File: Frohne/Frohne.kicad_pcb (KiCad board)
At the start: 4 copper layers, 100 x 100 mm, 215 parts, among them J1 ADC IN, J10 Conn_01x20_Socket, J11 SDR ANT, J12 SDR Out, J2 Conn_02x20_Counter_Clockwise, J3 Conn_02x20_Counter_Clockwise, J4 Conn_01x20_Socket, J5 Conn_01x02, J7 Conn_01x01_Pin, J8 BNC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

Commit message: Unconnected 29
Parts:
- removed J7: Conn_01x01_Pin, Connector_PinHeader_2.54mm:PinHeader_1x01_P2.54mm_Vertical
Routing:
- net GND: track 75.3 -> 120.2 mm
- net +4.7V: track 40.4 -> 54.8 mm
- net Net-(e1-EN): track 9.38 -> 15.2 mm
- net /Raspberry_Pi_Pico/GPIO12: track 13.5 -> 17.1 mm, vias 0 -> 1
- net +3.3V: track 23.6 -> 26.2 mm
- net /Raspberry_Pi_Pico/GPIO13: track 12.5 -> 14.7 mm, vias 0 -> 1
- net Net-(J4-Pin_5): track 0.00 -> 1.62 mm
- net Net-(J4-Pin_19): track 0.00 -> 1.59 mm
- net Net-(J2-Pin_17): track 5.69 -> 7.18 mm

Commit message: Unconnected 16
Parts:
- moved JP50 5.87 mm to (159.2, 33.1)
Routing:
- net Net-(JP19-B): track 22.6 -> 30.8 mm
- net +4.7V: track 54.8 -> 59.0 mm
- net Net-(FB5-Pad1): track 0.08 -> 4.22 mm
- net Net-(J10-Pin_1): track 0.00 -> 3.09 mm
- net Net-(C34-Pad1): track 0.00 -> 1.71 mm
- net Net-(J2-Pin_15): track 4.03 -> 5.69 mm
- net Net-(J4-Pin_2): track 0.00 -> 1.64 mm
- net Net-(J4-Pin_4): track 0.00 -> 1.63 mm
- net Net-(J4-Pin_7): track 0.00 -> 1.63 mm
- net Net-(J4-Pin_6): track 0.00 -> 1.62 mm
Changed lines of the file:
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@@
 	(footprint "Jumper:SolderJumper-2_P1.3mm_Open_RoundedPad1.0x1.5mm"
 		(layer "B.Cu")
-		(at 153.28 33.19 -90)
+		(at 159.15 33.11 -90)
 		(descr "SMD Solder Jumper, 1x1.5mm, rounded Pads, 0.3mm gap, open")
 		(tags "solder jumper open")
@@
 	)
 	(segment
+		(start 159.15 33.76)
+		(end 160.46 33.76)
+		(width 0.6)
+		(layer "B.Cu")
+		(net 13)
+	)
+	(segment
 		(start 161.1 34.06)
 		(end 160.92 34.06)
@@
 	)
 	(segment
+		(start 160.46 33.76)
+		(end 160.84 34.14)
+		(width 0.6)
+		(layer "B.Cu")
+		(net 13)
+	)
+	(segment
+		(start 172.22 32.35)
+		(end 172.035 32.535)
+		(width 0.4)
+		(layer "B.Cu")
+		(net 13)
+	)
+	(segment
 		(start 161.038 33.942)
 		(end 160.84 34.14)
@@
 	)
 	(segment
+		(start 174.31 32.35)
+		(end 172.22 32.35)
+		(width 0.4)
+		(layer "B.Cu")
+		(net 13)
+	)
+	(segment
 		(start 163.85 32.59)
 		(end 163.87 32.57)
@@
 	)
 	(segment
+		(start 121.3085 73.8115)
+		(end 121.3085 69.4615)
+		(width 0.127)
+		(layer "F.Cu")
+		(net 21)
+	)
+	(segment
 		(start 119.81 75.31)
 		(end 119.88 75.24)
@@
 		(net 21)
 	)
+	(segment
+		(start 119.88 75.24)
+		(end 121.3085 73.8115)
+		(width 0.127)
+		(layer "F.Cu")
+		(net 21)
+	)
+	(segment
+		(start 121.3085 69.4615)
+		(end 122.61 68.16)
+		(width 0.127)
+		(layer "F.Cu")
+		(net 21)
+	)
 	(via
 		(at 119.81 76.17)
@@
 	)
 	(segment
+		(start 142.8 45.25)
+		(end 144.35 45.25)
+		(width 0.127)
+		(layer "B.Cu")
+		(net 28)
+	)
+	(segment
+		(start 144.35 45.25)
+		(end 144.4 45.3)
+		(width 0.127)
+		(layer "B.Cu")
+		(net 28)
+	)
+	(segment
 		(start 146.77 125.12)
 		(end 149.56 125.12)
@@
 	)
 	(segment
+		(start 134.62 127.18)
+		(end 134.62 123.13)
+		(width 0.6)
+		(layer "F.Cu")
+		(net 30)
+	)
+	(segment
+		(start 134.62 123.13)
+		(end 134.68 123.07)
+		(width 0.6)
+		(layer "F.Cu")
+		(net 30)
+	)
+	(segment
 		(start 136.43 110.455)
 		(end 134.087 108.112)
@@
 	)
 	(segment
+		(start 126.32 123.88)
+		(end 126.32 122.4)
+		(width 0.127)
+		(layer "F.Cu")
+		(net 80)
+	)
+	(segment
+		(start 126.32 122.4)
+		(end 126.48 122.24)
+		(width 0.127)
+		(layer "F.Cu")
+		(net 80)
+	)
+	(segment
 		(start 128.9 103.94)
 		(end 128.81 103.85)
@@
 	)
 	(segment
+		(start 142.79 47.79)
+		(end 144.35 47.79)
+		(width 0.127)
+		(layer "B.Cu")
+		(net 82)
+	)
+	(segment
+		(start 144.35 47.79)
+		(end 144.4 47.84)
+		(width 0.127)
+		(layer "B.Cu")
+		(net 82)
+	)
+	(segment
 		(start 142.81 60.54)
 		(end 144.4 60.54)
@@
 	)
 	(segment
+		(start 141.51 68.16)
+		(end 139.856 68.16)
+		(width 0.127)
+		(layer "B.Cu")
+		(net 84)
+	)
+	(segment
 		(start 139.844 68.16)
 		(end 139.85 68.166)
@@
 	)
 	(segment
+		(start 139.856 68.16)
+		(end 139.85 68.166)
+		(width 0.127)
+		(layer "B.Cu")
+		(net 84)
+	)
+	(segment
 		(start 142.81 58)
 		(end 144.4 58)
@@
 	)
 	(segment
+		(start 144.36 35.1)
+		(end 144.4 35.14)
+		(width 0.127)
+		(layer "B.Cu")
+		(net 87)
+	)
+	(segment
+		(start 142.78 35.1)
+		(end 144.36 35.1)
+		(width 0.127)
+		(layer "B.Cu")
+		(net 87)
+	)
+	(segment
 		(start 141.51 78.32)
 		(end 135.745 78.32)
@@
 	)
 	(segment
+		(start 144.37 40.25)
+		(end 144.4 40.22)
+		(width 0.127)
+		(layer "B.Cu")
+		(net 95)
+	)
+	(segment
+		(start 142.78 40.25)
+		(end 144.37 40.25)
+		(width 0.127)
+		(layer "B.Cu")
+		(net 95)
+	)
+	(segment
 		(start 137.31 80.866)
 		(end 141.504 80.866)
@@
 	)
 	(segment
-		(start 118.505 126.765)
-		(end 118.53 126.79)
-		(width 0.127)
-		(layer "F.Cu")
-		(net 98)
-	)
-	(segment
 		(start 116.3945 126.7845)
 		(end 116.375 126.765)
@@
 	)
 	(segment
+		(start 159.15 32.46)
+		(end 160.59 32.46)
+		(width 0.6)
+		(layer "B.Cu")
+		(net 113)
+	)
+	(segment
+		(start 160.73 32.6)
+		(end 162.18 32.6)
+		(width 0.6)
+		(layer "B.Cu")
+		(net 113)
+	)
+	(segment
+		(start 160.59 32.46)
+		(end 160.73 32.6)
+		(width 0.6)
+		(layer "B.Cu")
+		(net 113)
+	)
+	(segment

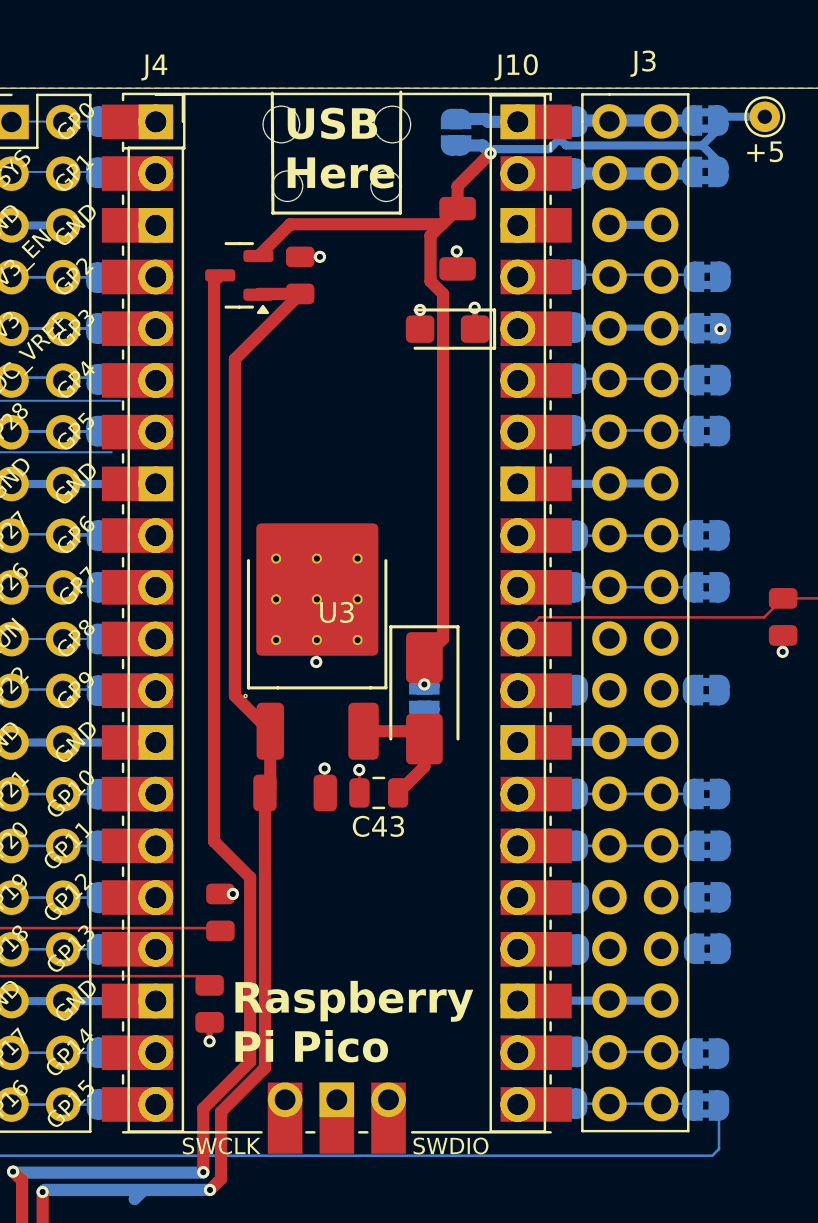
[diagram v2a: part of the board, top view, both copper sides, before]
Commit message: 0 Unconnected 53 Errors
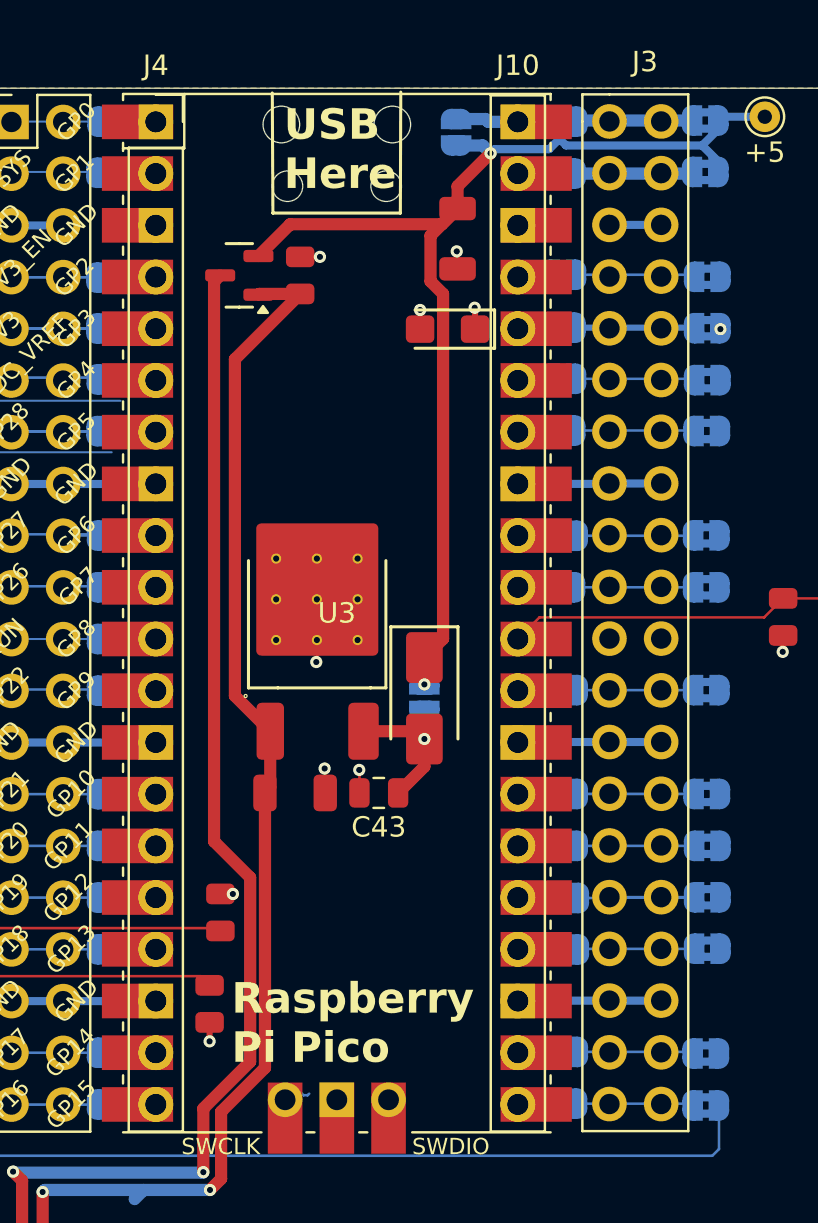
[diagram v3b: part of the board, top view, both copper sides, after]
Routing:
- net Net-(J3-Pin_16): track 0.00 -> 9.83 mm
- net Net-(J3-Pin_17): track 0.00 -> 5.67 mm
- net Net-(J3-Pin_12): track 0.00 -> 5.66 mm
- net GND: track 120.2 -> 123.8 mm
- net Net-(J10-Pin_16): track 0.00 -> 1.71 mm
- net Net-(J10-Pin_17): track 0.00 -> 1.70 mm
- net Net-(J10-Pin_12): track 0.00 -> 1.65 mm
- net Net-(J4-Pin_15): track 0.00 -> 1.59 mm
- net Net-(J4-Pin_1): track 0.00 -> 1.56 mm
- net Net-(J10-Pin_5): track 0.00 -> 1.55 mm
- net Net-(JP2-A): track 6.33 -> 7.71 mm, vias 0 -> 1
- net unconnected-(U3-SWCLK-Pad41): track 0.00 -> 1.37 mm
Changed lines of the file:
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@@
 	)
 	(segment
+		(start 152.33 59.08)
+		(end 152.33 55.57)
+		(width 0.127)
+		(layer "F.Cu")
+		(net 1)
+	)
+	(segment
 		(start 179.27 52.88)
 		(end 179.05 52.66)
@@
 	)
 	(segment
+		(start 152.28 59.13)
+		(end 152.33 59.08)
+		(width 0.127)
+		(layer "F.Cu")
+		(net 1)
+	)
+	(segment
 		(start 118.74 101.78)
 		(end 118.63 101.89)
@@
 	)
 	(segment
+		(start 151.27 80.63)
+		(end 151.568981 80.331019)
+		(width 0.127)
+		(layer "B.Cu")
+		(net 52)
+	)
+	(segment
+		(start 151.568981 80.331019)
+		(end 151.643962 80.406)
+		(width 0.127)
+		(layer "B.Cu")
+		(net 52)
+	)
+	(segment
+		(start 151.856038 80.406)
+		(end 151.931019 80.331019)
+		(width 0.127)
+		(layer "B.Cu")
+		(net 52)
+	)
+	(segment
+		(start 151.643962 80.406)
+		(end 151.856038 80.406)
+		(width 0.127)
+		(layer "B.Cu")
+		(net 52)
+	)
+	(segment
+		(start 150.75 80.63)
+		(end 151.27 80.63)
+		(width 0.127)
+		(layer "B.Cu")
+		(net 52)
+	)
+	(segment
 		(start 119.84 81.26)
 		(end 121.425 81.26)
@@
 		(net 69)
 	)
+	(via
+		(at 157.59 62.91)
+		(size 0.6)
+		(drill 0.3)
+		(layers "F.Cu" "B.Cu")
+		(net 69)
+	)
+	(segment
+		(start 157.59 61.53)
+		(end 157.59 62.91)
+		(width 0.6)
+		(layer "B.Cu")
+		(net 69)
+	)
 	(segment
 		(start 123.94 55.36)
@@
 	)
 	(segment
+		(start 142.85 32.6)
+		(end 142.84 32.59)
+		(width 0.127)
+		(layer "B.Cu")
+		(net 99)
+	)
+	(segment
+		(start 144.4 32.6)
+		(end 142.85 32.6)
+		(width 0.127)
+		(layer "B.Cu")
+		(net 99)
+	)
+	(segment
+		(start 142.81 68.16)
+		(end 144.4 68.16)
+		(width 0.127)
+		(layer "B.Cu")
+		(net 100)
+	)
+	(segment
 		(start 170.735 40.11)
 		(end 170.835 40.21)
@@
 	)
 	(segment
+		(start 163.71 42.71)
+		(end 162.23 42.71)
+		(width 0.3)
+		(layer "B.Cu")
+		(net 118)
+	)
+	(segment
+		(start 162.23 42.71)
+		(end 162.18 42.76)
+		(width 0.3)
+		(layer "B.Cu")
+		(net 118)
+	)
+	(segment
 		(start 163.66 45.3)
 		(end 163.74 45.22)
@@
 	)
 	(segment
+		(start 162.21 60.51)
+		(end 162.18 60.54)
+		(width 0.127)
+		(layer "B.Cu")
+		(net 123)
+	)
+	(segment
+		(start 163.82 60.51)
+		(end 162.21 60.51)
+		(width 0.127)
+		(layer "B.Cu")
+		(net 123)
+	)
+	(segment
 		(start 134.585 45.915)
 		(end 134.97 46.3)
@@
 	)
 	(segment
+		(start 170.785 60.51)
+		(end 165.12 60.51)
+		(width 0.127)
+		(layer "B.Cu")
+		(net 127)
+	)
+	(segment
 		(start 165.12 65.61)
 		(end 170.81 65.61)
@@
 	)
 	(segment
+		(start 166.675 70.685)
+		(end 170.835 70.685)
+		(width 0.127)
+		(layer "B.Cu")
+		(net 130)
+	)
+	(segment
+		(start 165.18 70.72)
+		(end 166.64 70.72)
+		(width 0.127)
+		(layer "B.Cu")
+		(net 130)
+	)
+	(segment
+		(start 166.64 70.72)
+		(end 166.675 70.685)
+		(width 0.127)
+		(layer "B.Cu")
+		(net 130)
+	)
+	(segment
+		(start 166.68 70.68)
+		(end 170.83 70.68)
+		(width 0.127)
+		(layer "B.Cu")
+		(net 130)
+	)
+	(segment
+		(start 170.83 70.68)
+		(end 170.835 70.685)
+		(width 0.127)
+		(layer "B.Cu")
+		(net 130)
+	)
+	(segment
+		(start 165.21 73.22)
+		(end 165.18 73.25)
+		(width 0.127)
+		(layer "B.Cu")
+		(net 131)
+	)
+	(segment
+		(start 166.68 73.22)
+		(end 165.21 73.22)
+		(width 0.127)
+		(layer "B.Cu")
+		(net 131)
+	)
+	(segment
+		(start 166.68 73.22)
+		(end 170.825 73.22)
+		(width 0.127)
+		(layer "B.Cu")
+		(net 131)
+	)
+	(segment
+		(start 170.825 73.22)
+		(end 170.835 73.21)
+		(width 0.127)
+		(layer "B.Cu")
+		(net 131)
+	)
+	(segment
 		(start 165.13 78.28)
 		(end 170.68 78.28)
@@
 	)
 	(segment
+		(start 162.2 70.72)
+		(end 162.18 70.7)
+		(width 0.127)
+		(layer "B.Cu")
+		(net 163)
+	)
+	(segment
+		(start 163.88 70.72)
+		(end 162.2 70.72)
+		(width 0.127)
+		(layer "B.Cu")
+		(net 163)
+	)
+	(segment
+		(start 163.88 73.25)
+		(end 162.19 73.25)
+		(width 0.127)
+		(layer "B.Cu")
+		(net 164)
+	)
+	(segment
+		(start 162.19 73.25)
+		(end 162.18 73.24)
+		(width 0.127)
+		(layer "B.Cu")
+		(net 164)
+	)
+	(segment

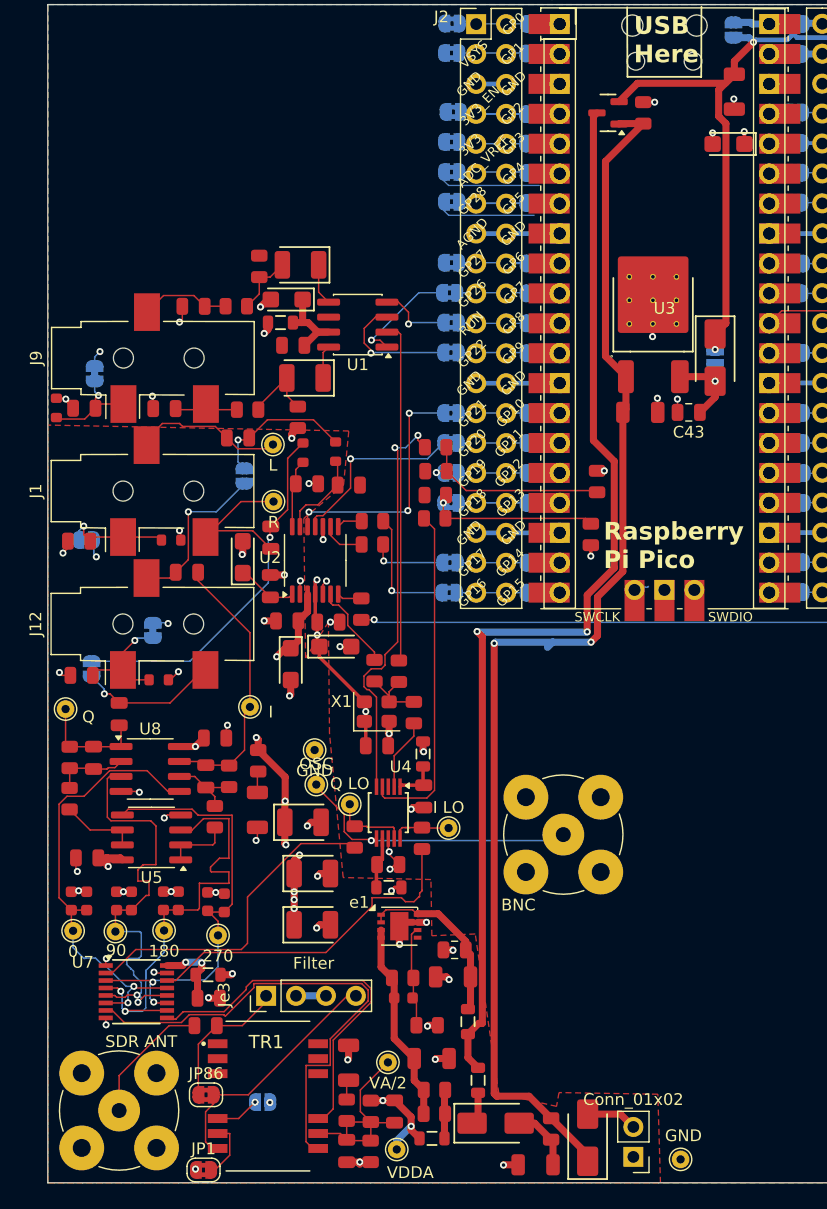
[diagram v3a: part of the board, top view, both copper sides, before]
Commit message: 0 unconnected, 0 Errors 411+ warnings
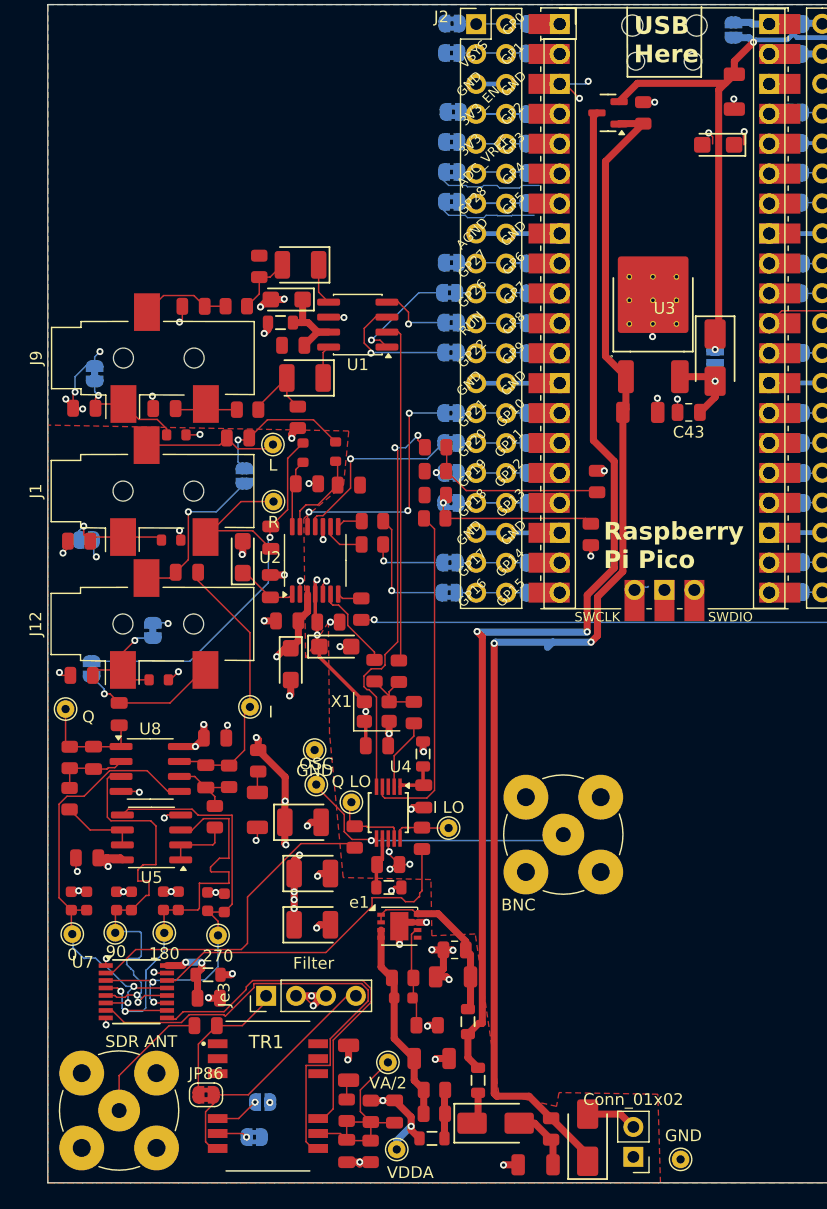
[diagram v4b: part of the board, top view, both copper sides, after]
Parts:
- JP1: moved to B.Cu
- moved R19 10.4 mm to (111.9, 67.5), turned to 0 degrees
- moved JP1 5.13 mm to (118.5, 127.1), turned to 180 degrees
- moved C39 0.88 mm to (157.8, 42.9)
- moved TP14 0.29 mm to (103.0, 109.8)
- moved TP4 0.22 mm to (126.7, 98.7)
- moved TP6 0.21 mm to (110.8, 109.7)
- moved TP16 0.11 mm to (106.7, 109.7)
- moved R27 0.05 mm to (133.8, 70.5)
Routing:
- net GND: track 123.8 -> 145.0 mm, vias 59 -> 69
- net Net-(JP1-B): track 4.95 -> 2.58 mm, vias 0 -> 1
- net Net-(e3-B): track 8.79 -> 10.1 mm
- net VDDA: track 38.2 -> 39.3 mm, vias 13 -> 14
- net Net-(C3-Pad2): track 12.8 -> 12.0 mm
- net +4.7V: track 59.0 -> 58.5 mm
